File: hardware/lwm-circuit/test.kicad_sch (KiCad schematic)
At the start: 29 parts, among them J1 Analog, J2 Digital, J4 Micro_SD_Card_Det_Hirose_DM3AT, U1 MCP23017x-x-ML, U2 MCP23017x-x-ML, U3 MCP23017x-x-ML, U4 MCP23017x-x-ML, U5 MCP23017x-x-ML, U6 254

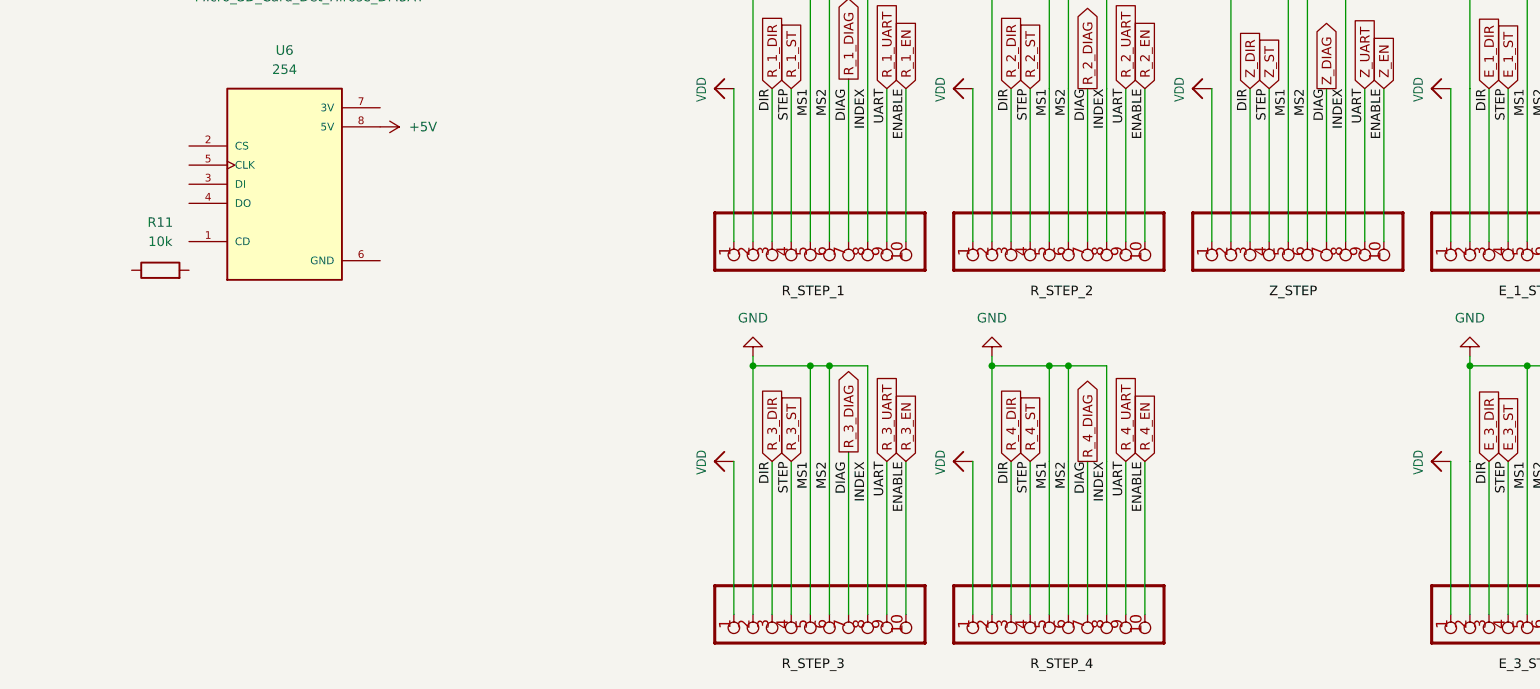
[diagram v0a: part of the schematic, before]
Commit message: Added base plate driver
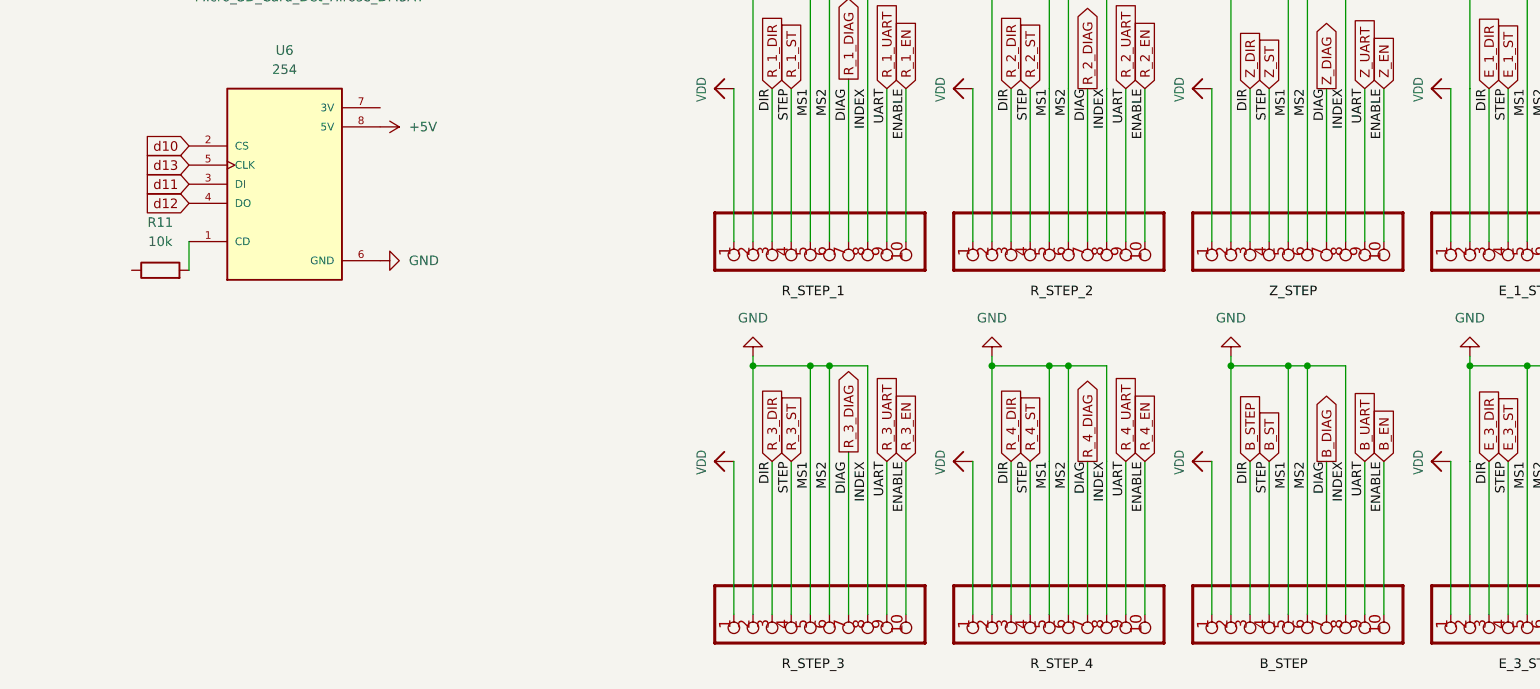
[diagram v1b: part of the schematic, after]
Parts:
- added JP9: HEADER-1X1070MIL, Adafruit TMC2209 Stepper Motor Driver:1X10_ROUND70, symbol Adafruit TMC2209 Stepper Motor Driver-eagle-import:HEADER-1X1070MIL
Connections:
- net GND: now also U6.6 (GND), JP9.2, JP9.5, JP9.6, JP9.8
- net VDD: now also JP9.1
- net at U6.1 (CD): now also R11.2
- net d10: now reaches U6.2 (CS)
- net d11: now reaches U6.3 (DI)
- net d12: now reaches U6.4 (DO)
- net d13: now reaches U6.5 (CLK)
- net E_1_DIAG renamed B_DIAG
- net B_DIAG: now also JP9.7
- net E_1_DIR renamed B_STEP
- net B_STEP: now also JP9.3
- net E_1_EN renamed B_EN
- net B_EN: now also JP9.10
- net E_1_ST renamed B_ST
- net B_ST: now also JP9.4
- net E_1_UART renamed B_UART
- net B_UART: now also JP9.9
